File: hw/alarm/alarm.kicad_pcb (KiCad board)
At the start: 2 copper layers, 71 x 73 mm, 73 parts, among them IC3 SHT40-BD1B-R2, IC6 MAX31328NELB+, J10 Conn_01x03, J2 FFC2B35-24-T, J3 975, J4 SM04B-SRSS-TB_LF__SN__P_, J5 Conn_01x01_Pin, J6 Conn_01x05, J9 Conn_01x05, Q1 DMG2305UX-7, Q2 2SC5585TL, Q3 Si1308EDL-T1-GE3, Q4 DMG2305UX-7, U1 RaspberryPi_Pico, U2 PEC11R-4215F-S0024, U4 AS1115-BSST, U5 TDCR1060M

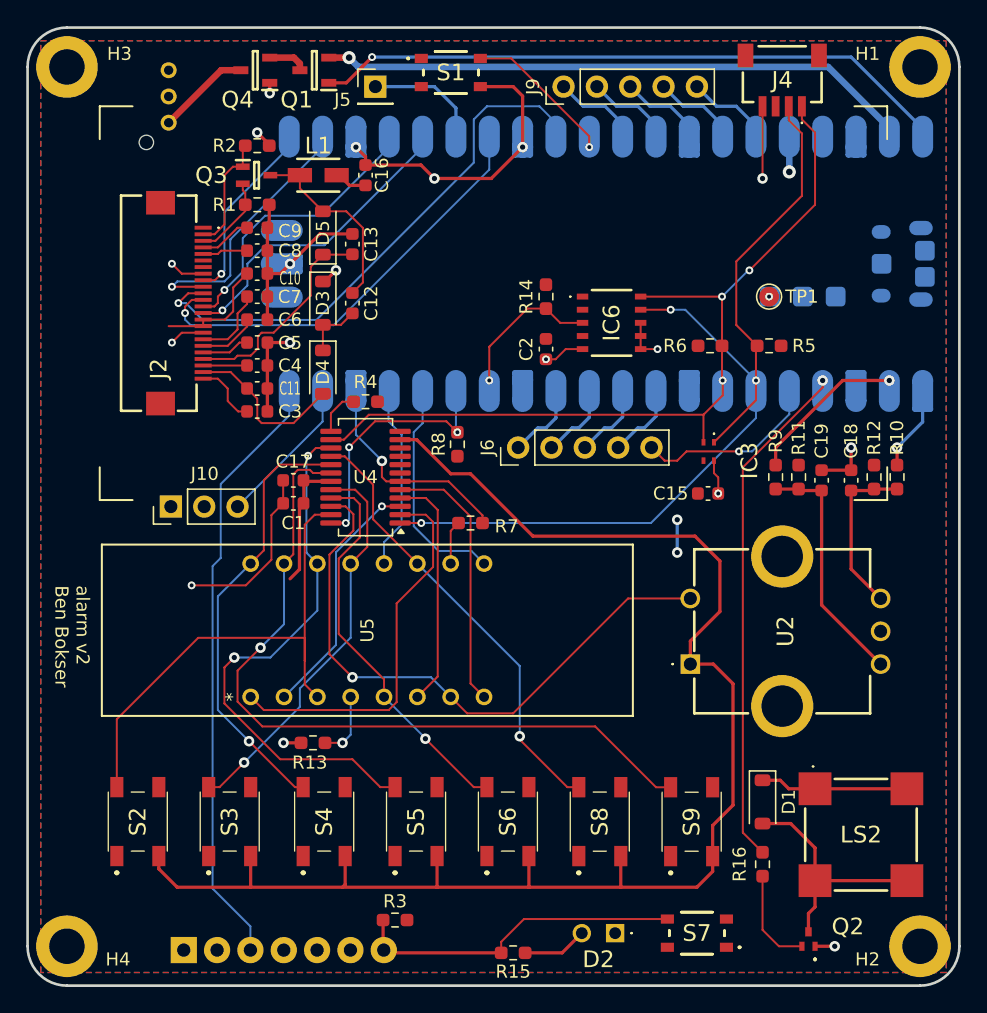
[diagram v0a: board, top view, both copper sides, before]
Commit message: Add LCSC PNs, Replace through-hole breakouts with SMD header, reannotate
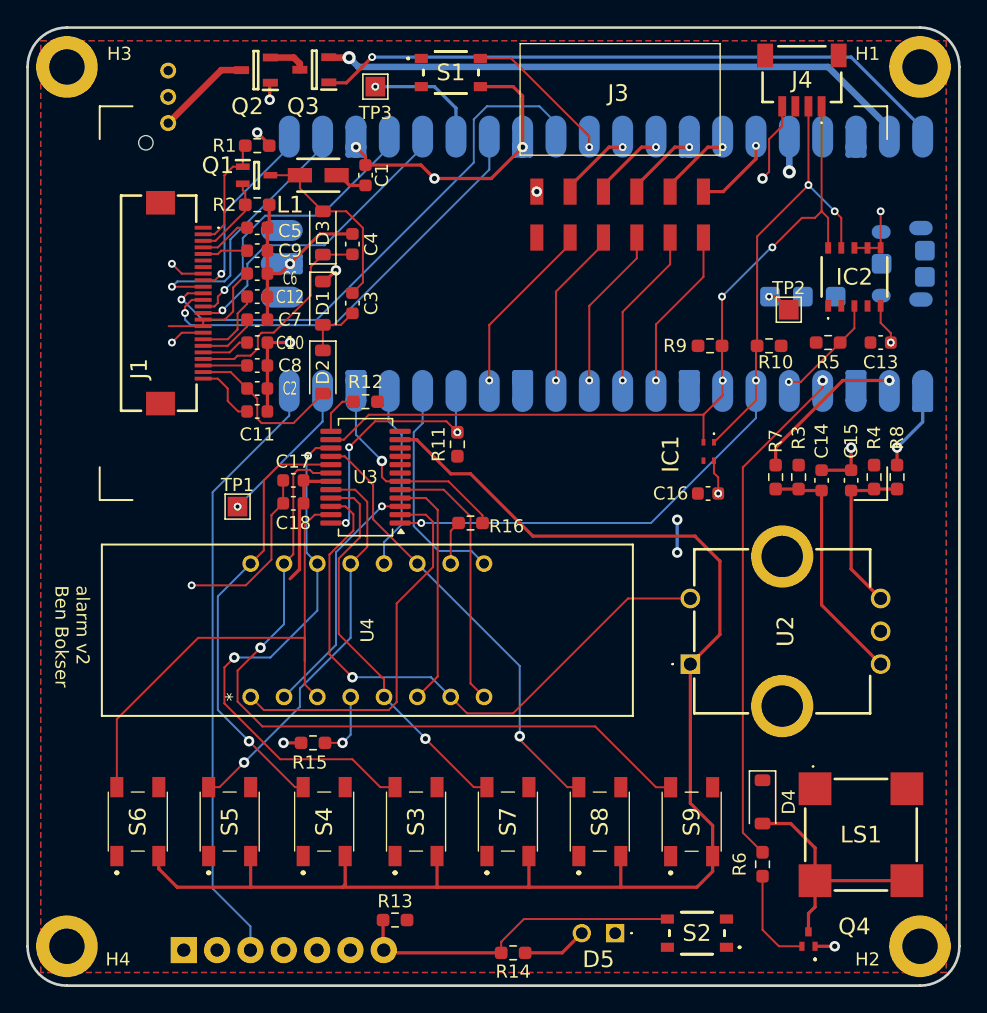
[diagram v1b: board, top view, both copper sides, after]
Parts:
- removed J10: Conn_01x03, Connector_PinHeader_2.54mm:PinHeader_1x03_P2.54mm_Vertical
- removed J5: Conn_01x01_Pin, Connector_PinHeader_2.54mm:PinHeader_1x01_P2.54mm_Vertical
- removed J6, J9: Conn_01x05, Connector_PinHeader_2.54mm:PinHeader_1x05_P2.54mm_Vertical
- removed the Q1 at (144.3, 64.8)
- removed the Q4 at (139.8, 64.8)
- added J2: 975, SamacSys_Parts:975, B.Cu at (133.2, 68.8)
- added Q2: DMG2305UX-7, SamacSys_Parts:SOT96P240X115-3N, F.Cu at (139.9, 64.7)
- added Q3: DMG2305UX-7, SamacSys_Parts:SOT96P240X115-3N, F.Cu at (144.3, 64.7)
- added TP1: TestPoint, TestPoint:TestPoint_Pad_1.5x1.5mm, F.Cu at (138.5, 98.0)
- added TP3: TestPoint, TestPoint:TestPoint_Pad_1.5x1.5mm, F.Cu at (149.0, 66.0)
- J3: value 975 -> M20-7920642R; footprint SamacSys_Parts:975 -> SamacSys_Parts:M207920642R; moved to F.Cu
- R12: renamed from R4; value 13.9kΩ -> 14kΩ
- TP2: renamed from TP1; footprint TestPoint:TestPoint_Pad_D1.5mm -> TestPoint:TestPoint_Pad_1.5x1.5mm
- moved J3 34.5 mm to (167.7, 70.6), turned to 0 degrees
- moved C13 25.5 mm to (187.5, 85.5), turned to 0 degrees
- moved R5 21.8 mm to (183.5, 85.5), turned to 0 degrees
- moved IC2 18.8 mm to (185.5, 80.5), turned to 0 degrees
- moved TP2 1.80 mm to (180.5, 83.0)
- moved J4 1.50 mm to (181.5, 65.2)
- renumbered C16 to C1, C5 to C10, C3 to C11, C7 to C12, C2 to C13, C19 to C14, C18 to C15, C15 to C16, C1 to C18, C11 to C2, C12 to C3, C13 to C4, C9 to C5, C10 to C6, C6 to C7, C4 to C8, C8 to C9, D3 to D1, D4 to D2, D5 to D3, D1 to D4, D2 to D5, IC3 to IC1, IC6 to IC2, J2 to J1, LS2 to LS1, Q3 to Q1, Q2 to Q4, R2 to R1, R5 to R10, R8 to R11, R3 to R13, R15 to R14, R13 to R15, R7 to R16, R1 to R2, R11 to R3, R12 to R4, R14 to R5, R16 to R6, R9 to R7, R10 to R8, R6 to R9, S7 to S2, S5 to S3, S3 to S5, S2 to S6, S6 to S7, U4 to U3, U5 to U4
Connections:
- J3 pad 1: Net-(J3-+) -> +3.3V
- J3 pad 2: unconnected-(J3-NC-Pad2) -> GND
- J3 pad 3: GND -> /GP14
- U1 pad 10: Net-(J6-Pin_3) -> /GP7
- U1 pad 11: Net-(J6-Pin_2) -> /GP8
- U1 pad 12: Net-(J6-Pin_1) -> /GP9
- U1 pad 14: /RTC_INT -> /GP14
- U1 pad 31: Net-(J9-Pin_1) -> /ADC0
- U1 pad 32: Net-(J9-Pin_2) -> /ADC1
- U1 pad 33: Net-(J9-Pin_3) -> /AGND
- U1 pad 34: Net-(J9-Pin_4) -> /ADC2
- U1 pad 35: Net-(J9-Pin_5) -> /ADC_VREF
- U1 pad 39: Net-(Q1-S) -> /VSYS
- U1 pad 40: Net-(Q1-G) -> /VBUS
- U1 pad 5: Net-(J6-Pin_5) -> /RTC_INT
- U1 pad 9: Net-(J6-Pin_4) -> /GP6
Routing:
- net Net-(Q1-G): track 49.7 -> 0.00 mm, vias 1 -> 0
- net /VBUS: track 0.00 -> 49.7 mm, vias 0 -> 1
- net /VSYS: track 0.00 -> 46.4 mm, vias 0 -> 1
- net Net-(Q1-S): track 46.4 -> 0.00 mm, vias 1 -> 0
- net Net-(J6-Pin_5): track 15.0 -> 0.00 mm, vias 1 -> 0
- net /GP14: track 0.00 -> 13.4 mm, vias 0 -> 1
- net /GP7: track 0.00 -> 12.4 mm, vias 0 -> 1
- net /GP9: track 0.00 -> 12.4 mm, vias 0 -> 1
- net /GP6: track 0.00 -> 12.4 mm, vias 0 -> 1
- net /GP8: track 0.00 -> 12.4 mm, vias 0 -> 1
- net +3.3V: track 37.2 -> 25.9 mm
- net Net-(J9-Pin_1): track 7.45 -> 0.00 mm
- net Net-(J9-Pin_2): track 7.42 -> 0.00 mm
- net Net-(J9-Pin_3): track 7.39 -> 0.00 mm
- net Net-(J9-Pin_4): track 7.38 -> 0.00 mm
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
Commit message: Start work on v3.0
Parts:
- removed S6: PTS647SM70SMTR2LFS, SamacSys_Parts:PTS647SM38SMTR2LFS
- removed U2: PEC11R-4215F-S0024, SamacSys_Parts:PEC11R4215FS0024
- added IC3: PEC11S-929K-S0015, SamacSys_Parts:PEC11S929KS0015, F.Cu at (180.0, 107.5)
- S3, S4, S5, S7, S8, S9: value PTS647SM70SMTR2LFS -> TL3301BF260QJ; footprint SamacSys_Parts:PTS647SM38SMTR2LFS -> SamacSys_Parts:TL3301BF260QJ
- moved S4 14.1 mm to (131.0, 122.0), turned to -90 degrees
- moved D4 9.95 mm to (180.5, 130.2), turned to 0 degrees
- moved R13 9.01 mm to (159.5, 130.0)
- moved R6 7.52 mm to (180.5, 132.5), turned to 0 degrees
- moved S3 4.10 mm to (148.0, 122.0), turned to -90 degrees
- moved Q4 3.00 mm to (185.0, 130.9)
- moved S7 2.60 mm to (156.5, 122.0), turned to -90 degrees
- moved S5 1.60 mm to (139.5, 122.0), turned to -90 degrees
- moved S8 1.10 mm to (165.0, 122.0), turned to -90 degrees
- moved S9 0.40 mm to (173.5, 122.0), turned to -90 degrees
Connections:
- R13 pad 2: +3.3V -> Net-(S2-NO_2)
- S2 pad 4: Net-(A1-KEY) -> Net-(S2-NO_2)
- S3 pad 2: Net-(U3-SEGA) -> unconnected-(S3-Pad2)
- S3 pad 3: /Enc_D -> Net-(U3-SEGA)
- S3 pad 4: unconnected-(S3-Pad4) -> /Enc_D
- S4 pad 1: unconnected-(S4-Pad1) -> Net-(U3-SEGB)
- S4 pad 2: Net-(U3-SEGB) -> unconnected-(S4-Pad2)
- S4 pad 3: /Enc_D -> unconnected-(S4-Pad3)
- S4 pad 4: unconnected-(S4-Pad4) -> /Enc_D
- S5 pad 1: unconnected-(S5-Pad1) -> Net-(U3-SEGC)
- S5 pad 2: Net-(U3-SEGC) -> unconnected-(S5-Pad2)
- S5 pad 3: /Enc_D -> unconnected-(S5-Pad3)
- S5 pad 4: unconnected-(S5-Pad4) -> /Enc_D
- S7 pad 1: unconnected-(S7-Pad1) -> Net-(U3-SEGE)
- S7 pad 2: Net-(U3-SEGE) -> unconnected-(S7-Pad2)
- S7 pad 3: /Enc_D -> unconnected-(S7-Pad3)
- S7 pad 4: unconnected-(S7-Pad4) -> /Enc_D
- S8 pad 1: unconnected-(S8-Pad1) -> Net-(U3-SEGF)
- S8 pad 2: Net-(U3-SEGF) -> unconnected-(S8-Pad2)
- S8 pad 3: /Enc_D -> unconnected-(S8-Pad3)
- S8 pad 4: unconnected-(S8-Pad4) -> /Enc_D
- S9 pad 1: unconnected-(S9-Pad1) -> Net-(U3-SEGG)
- S9 pad 2: Net-(U3-SEGG) -> unconnected-(S9-Pad2)
- S9 pad 3: /Enc_D -> unconnected-(S9-Pad3)
- S9 pad 4: unconnected-(S9-Pad4) -> /Enc_D
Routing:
- net Net-(U3-SEGD): track 39.6 -> 15.8 mm
- net Net-(A1-KEY): track 25.6 -> 11.1 mm
- net Net-(S2-NO_2): track 0.00 -> 11.4 mm
- net /Buzzer: track 39.1 -> 48.0 mm
- net Net-(D4-A): track 18.4 -> 13.8 mm
- net Net-(Q4-B): track 7.61 -> 3.79 mm
- net Net-(U3-SEGB): track 33.5 -> 36.2 mm, vias 1 -> 0
- net Net-(IC3-CCW): track 18.6 -> 20.5 mm
- net Net-(U3-SEGE): track 29.9 -> 28.2 mm
- net +3.3V: track 25.9 -> 27.3 mm
- net Net-(U3-SEGG): track 57.9 -> 59.1 mm
- net Net-(IC3-CW): track 12.6 -> 13.4 mm
- net GND: vias 20 -> 21

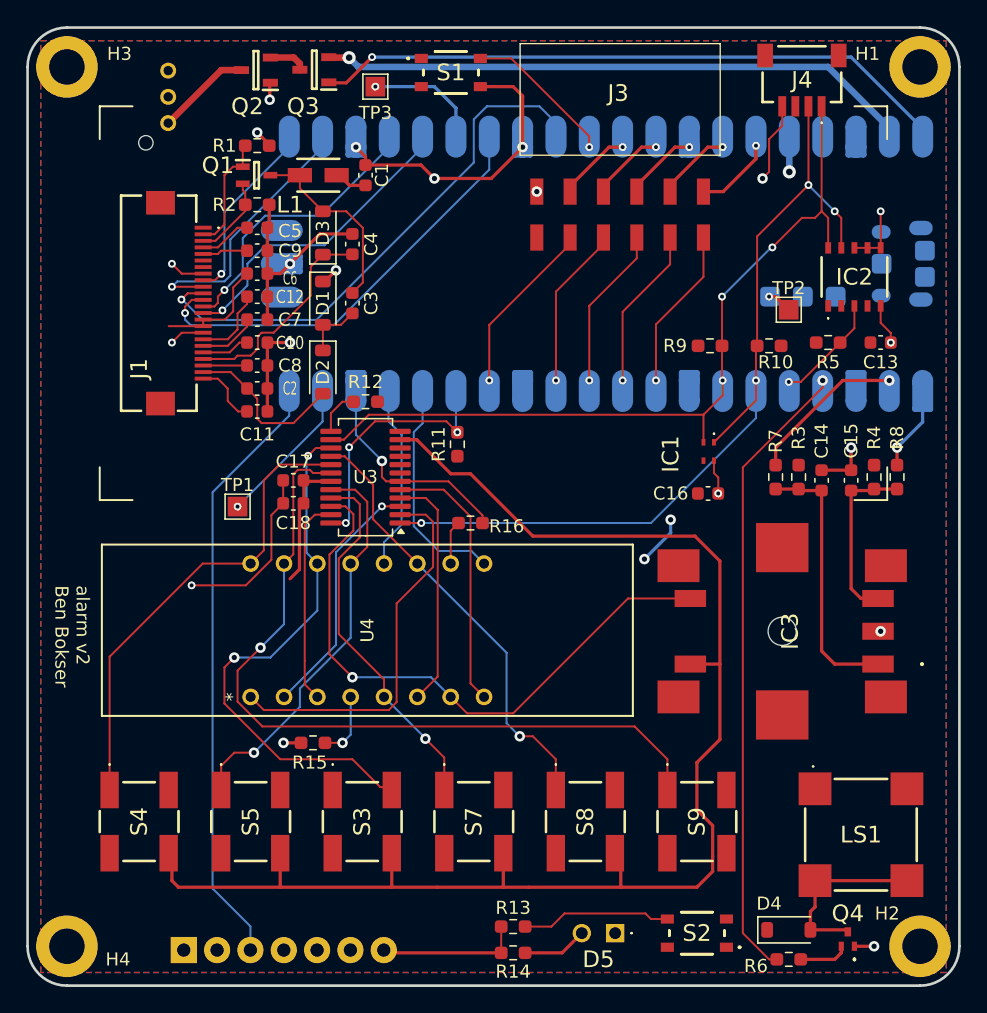
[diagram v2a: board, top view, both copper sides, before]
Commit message: Add front plate
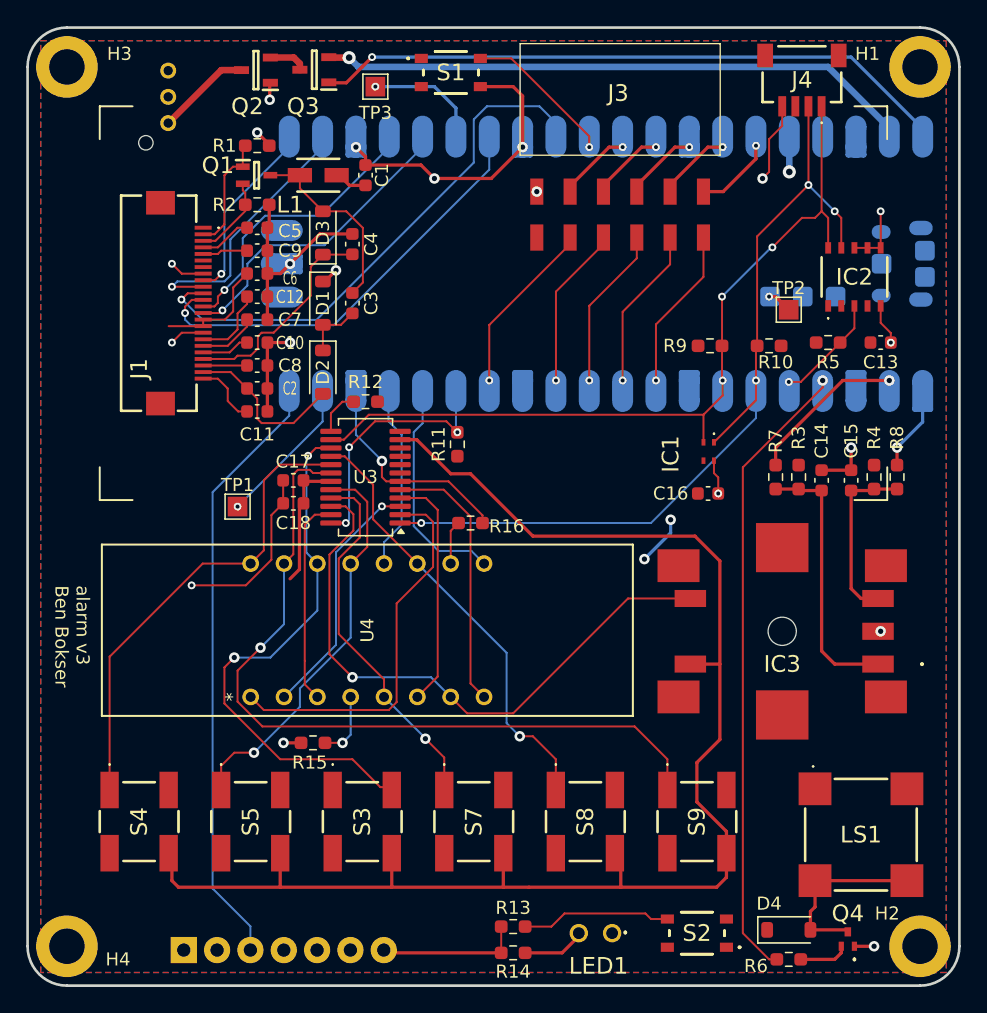
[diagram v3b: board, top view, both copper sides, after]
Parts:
- removed D5: LED, SamacSys_Parts:WP710A10LID
- added LED1: WP424IDT, SamacSys_Parts:WP424IDT, F.Cu at (167.0, 130.5)
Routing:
- net /Enc_D: track 109.4 -> 111.1 mm
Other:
- board text added: "alarm v3 Ben Bokser"
- board text removed: "alarm v2 Ben Bokser"

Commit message: Add front and rear plate
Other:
- board text added: "persuasive_waker v3 Ben Bokser"
- board text removed: "alarm v3 Ben Bokser"
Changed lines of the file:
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@@
 			)
 		)
-		(property "Footprint" "TL3301BF260QJ"
+		(property "Footprint" "SamacSys_Parts:TL3301BF260QJ"
 			(at 0 0 -90)
 			(unlocked yes)
@@
 			)
 		)
-		(property "Footprint" "TL3301BF260QJ"
+		(property "Footprint" "SamacSys_Parts:TL3301BF260QJ"
 			(at 0 0 -90)
 			(unlocked yes)
@@
 			)
 		)
-		(property "Footprint" "WP424IDT"
+		(property "Footprint" "SamacSys_Parts:WP424IDT"
 			(at 0 0 -90)
 			(unlocked yes)
@@
 			)
 		)
-		(property "Footprint" "TL3301BF260QJ"
+		(property "Footprint" "SamacSys_Parts:TL3301BF260QJ"
 			(at 0 0 -90)
 			(unlocked yes)
@@
 		(tags "SOD-123")
 		(property "Reference" "D4"
-			(at -1.5 -2 360)
+			(at -1.5 -2 0)
 			(layer "F.SilkS")
 			(effects
@@
 		)
 		(property "Value" "MBR0530"
-			(at 0 2.1 360)
+			(at 0 2.1 0)
 			(layer "F.Fab")
 			(effects
@@
 		)
 		(fp_text user "${REFERENCE}"
-			(at 0 -2 360)
+			(at 0 -2 0)
 			(layer "F.Fab")
 			(effects
@@
 		(tags "resistor handsolder")
 		(property "Reference" "R13"
-			(at 0 -1.43 360)
+			(at 0 -1.43 0)
 			(layer "F.SilkS")
 			(effects
@@
 		)
 		(property "Value" "1kΩ"
-			(at 0 1.43 360)
+			(at 0 1.43 0)
 			(layer "F.Fab")
 			(effects
@@
 		)
 		(fp_text user "${REFERENCE}"
-			(at 0 0 360)
+			(at 0 0 0)
 			(layer "F.Fab")
 			(effects
@@
 			)
 		)
-		(property "Footprint" "PEC11S929KS0015"
+		(property "Footprint" "SamacSys_Parts:PEC11S929KS0015"
 			(at 0 0 90)
 			(unlocked yes)
@@
 			)
 		)
-		(property "Footprint" "TL3301BF260QJ"
+		(property "Footprint" "SamacSys_Parts:TL3301BF260QJ"
 			(at 0 0 -90)
 			(unlocked yes)
@@
 		(tags "resistor handsolder")
 		(property "Reference" "R6"
-			(at -2.5 0.5 360)
+			(at -2.5 0.5 0)
 			(layer "F.SilkS")
 			(effects
@@
 		)
 		(property "Value" "180Ω"
-			(at 0 1.43 360)
+			(at 0 1.43 0)
 			(layer "F.Fab")
 			(effects
@@
 		)
 		(fp_text user "${REFERENCE}"
-			(at 0 0 360)
+			(at 0 0 0)
 			(layer "F.Fab")
 			(effects
@@
 			)
 		)
-		(property "Footprint" "TL3301BF260QJ"
+		(property "Footprint" "SamacSys_Parts:TL3301BF260QJ"
 			(at 0 0 -90)
 			(unlocked yes)
@@
 			)
 		)
-		(property "Footprint" "TL3301BF260QJ"
+		(property "Footprint" "SamacSys_Parts:TL3301BF260QJ"
 			(at 0 0 -90)
 			(unlocked yes)
@@
 		(layer "F.Fab")
 	)
-	(gr_text "alarm v3\nBen Bokser"
-		(at 124.5 104 270)
+	(gr_text "persuasive_waker v3\nBen Bokser"
+		(at 124.5 98.5 270)
 		(layer "F.SilkS")
 		(effects

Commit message: Fix S3 wiring mistake and update library paths
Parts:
- renumbered S7 to S6, S8 to S7, S9 to S8, U3 to U2, U4 to U3
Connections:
- S3 pad 1: unconnected-(S3-Pad1) -> Net-(U2-SEGA)
- S3 pad 3: Net-(U3-SEGA) -> unconnected-(S3-Pad3)
- U2 pad 15: Net-(U3-SEGA) -> Net-(U2-SEGA)
- U3 pad 14: Net-(U3-SEGA) -> Net-(U2-SEGA)
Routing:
- net Net-(U3-SEGA): track 41.4 -> 0.00 mm, vias 2 -> 0
- net Net-(U2-SEGA): track 0.00 -> 37.7 mm, vias 0 -> 2
